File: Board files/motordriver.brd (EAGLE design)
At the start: 30.1 x 44.5 mm, 13 parts, among them Q1 IPB034N03L, U1 VNH5019A

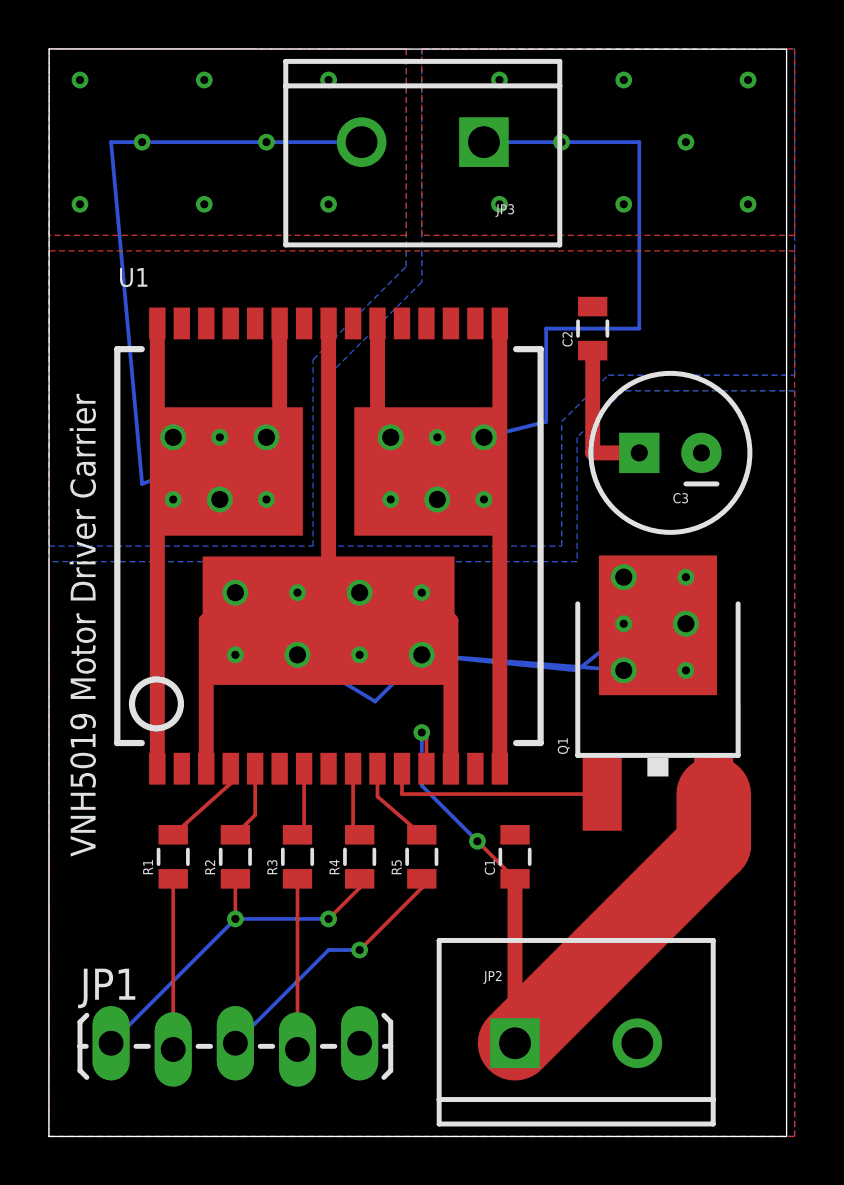
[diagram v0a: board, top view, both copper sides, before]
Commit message: Modified motor driver layout
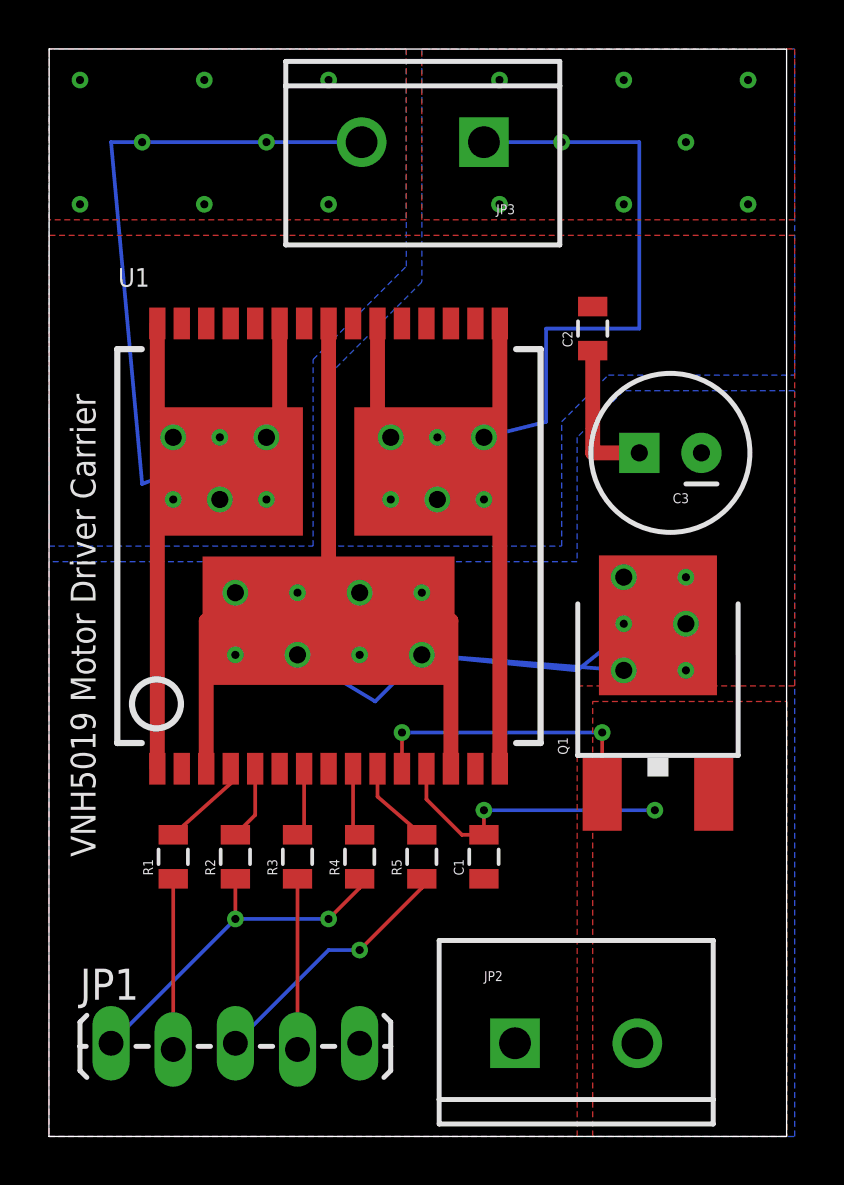
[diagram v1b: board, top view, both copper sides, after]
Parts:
- moved C1 1.27 mm to (17.8, 11.4)
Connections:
- net GND: now also C1.1, JP2.1; no longer C1.2, JP2.2
- net VIN: now also C1.2, JP2.2; no longer C1.1, JP2.1
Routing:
- net VIN: track 29.4 -> 12.5 mm
- net N$4: track 9.22 -> 12.2 mm, vias 0 -> 2
- added copper zone on layer 1, net VIN
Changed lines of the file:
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@@
 <attribute name="PROD_ID" value="TRANS-09984" x="24.892" y="19.304" size="1.778" layer="27" display="off"/>
 </element>
-<element name="C1" library="SparkFun-Capacitors" package="0805" value="0.1uF" x="19.05" y="11.43" rot="R90"/>
+<element name="C1" library="SparkFun-Capacitors" package="0805" value="0.1uF" x="17.78" y="11.43" rot="R90"/>
 <element name="C2" library="SparkFun-Capacitors" package="0805" value="0.1uF" x="22.225" y="33.02" rot="R90"/>
 <element name="C3" library="SparkFun-Capacitors" package="CPOL-RADIAL-100UF-25V" value="47uF" x="25.4" y="27.94" rot="R180"/>
@@
 <signals>
 <signal name="GND">
-<contactref element="JP2" pad="2"/>
+<contactref element="JP2" pad="1"/>
 <contactref element="JP1" pad="5"/>
 <contactref element="U1" pad="26"/>
@@
 <contactref element="U1" pad="19"/>
 <contactref element="U1" pad="20"/>
-<contactref element="C1" pad="2"/>
+<contactref element="C1" pad="1"/>
 <contactref element="C2" pad="2"/>
 <contactref element="C3" pad="2"/>
-<polygon width="0.3048" layer="1">
+<polygon width="0.254" layer="1">
 <vertex x="0" y="0"/>
-<vertex x="30.48" y="0"/>
-<vertex x="30.48" y="36.195"/>
-<vertex x="0" y="36.195"/>
+<vertex x="21.59" y="0"/>
+<vertex x="21.59" y="18.415"/>
+<vertex x="30.48" y="18.415"/>
+<vertex x="30.48" y="36.83"/>
+<vertex x="0" y="36.83"/>
 </polygon>
 </signal>
 <signal name="VIN">
-<contactref element="JP2" pad="1"/>
+<contactref element="JP2" pad="2"/>
 <contactref element="Q1" pad="3"/>
 <contactref element="U1" pad="12"/>
-<contactref element="C1" pad="1"/>
-<wire x1="19.05" y1="3.81" x2="19.05" y2="10.53" width="0.6096" layer="1"/>
-<wire x1="19.05" y1="10.53" x2="17.515" y2="12.065" width="0.1524" layer="1"/>
-<via x="17.515" y="12.065" extent="1-16" drill="0.3302"/>
-<wire x1="17.515" y1="12.065" x2="15.24" y2="14.34" width="0.1524" layer="16"/>
-<wire x1="15.24" y1="14.34" x2="15.24" y2="16.51" width="0.1524" layer="16"/>
-<via x="15.24" y="16.51" extent="1-16" drill="0.3302"/>
-<wire x1="15.24" y1="16.51" x2="15.43" y2="16.32" width="0.1524" layer="1"/>
-<wire x1="15.43" y1="16.32" x2="15.43" y2="15.03" width="0.1524" layer="1"/>
-<wire x1="27.172" y1="13.994" x2="27.172" y2="11.932" width="3.048" layer="1"/>
-<wire x1="27.172" y1="11.932" x2="19.05" y2="3.81" width="3.048" layer="1"/>
+<contactref element="C1" pad="2"/>
+<wire x1="15.43" y1="15.03" x2="15.43" y2="15.05" width="0.1524" layer="1"/>
+<wire x1="15.43" y1="15.05" x2="15.24" y2="15.24" width="0.1524" layer="1"/>
+<wire x1="15.43" y1="15.03" x2="15.43" y2="13.78" width="0.1524" layer="1"/>
+<wire x1="15.43" y1="13.78" x2="16.88" y2="12.33" width="0.1524" layer="1"/>
+<wire x1="16.88" y1="12.33" x2="17.78" y2="12.33" width="0.1524" layer="1"/>
+<polygon width="0.254" layer="1">
+<vertex x="30.1625" y="0"/>
+<vertex x="22.225" y="0"/>
+<vertex x="22.225" y="17.78"/>
+<vertex x="30.1625" y="17.78"/>
+</polygon>
+<wire x1="17.78" y1="12.33" x2="17.78" y2="13.335" width="0.1524" layer="1"/>
+<via x="17.78" y="13.335" extent="1-16" drill="0.3302"/>
+<wire x1="17.78" y1="13.335" x2="24.765" y2="13.335" width="0.1524" layer="16"/>
+<via x="24.765" y="13.335" extent="1-16" drill="0.3302"/>
 </signal>
 <signal name="OUTB">
@@
 <polygon width="0.3048" layer="1">
 <vertex x="30.48" y="44.45"/>
-<vertex x="30.48" y="36.83"/>
-<vertex x="15.24" y="36.83"/>
+<vertex x="30.48" y="37.465"/>
+<vertex x="15.24" y="37.465"/>
 <vertex x="15.24" y="44.45"/>
 </polygon>
@@
 <vertex x="0" y="44.45"/>
 <vertex x="14.605" y="44.45"/>
-<vertex x="14.605" y="36.83"/>
-<vertex x="0" y="36.83"/>
+<vertex x="14.605" y="37.465"/>
+<vertex x="0" y="37.465"/>
 </polygon>
 <via x="3.81" y="40.64" extent="1-16" drill="0.3302"/>
@@
 <contactref element="U1" pad="11"/>
 <contactref element="Q1" pad="1"/>
-<wire x1="14.43" y1="15.03" x2="14.43" y2="13.994" width="0.1524" layer="1"/>
-<wire x1="14.43" y1="13.994" x2="22.612" y2="13.994" width="0.1524" layer="1"/>
+<wire x1="14.43" y1="15.03" x2="14.43" y2="16.51" width="0.1524" layer="1"/>
+<via x="14.43" y="16.51" extent="1-16" drill="0.3302"/>
+<wire x1="14.43" y1="16.51" x2="22.612" y2="16.51" width="0.1524" layer="16"/>
+<via x="22.612" y="16.51" extent="1-16" drill="0.3302"/>
+<wire x1="22.612" y1="16.51" x2="22.612" y2="13.994" width="0.1524" layer="1"/>
 </signal>
 <signal name="VCC">
